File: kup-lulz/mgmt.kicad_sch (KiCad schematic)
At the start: 24 parts, among them J37 XILINX_JTAG, J38 PMOD_HOST, J39 CONN_01X03, U14 STM32L431VxIx, U15 AT24MAC402, U9 XILINX_ULTRASCALEPLUS_B676

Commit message: Continued MCU fanout
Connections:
- net SFP1_MOD_ABS: now also U14.D12 (PC9); no longer U14.G1 (PH1)
- net SFP1_RS0: now also U14.E12 (PC6); no longer U14.M5 (PB0)
- net SFP1_RS1: now also U14.J12 (PD10); no longer U14.M8 (PE9)
- net SFP1_RX_LOS: now also U14.H12 (PD13); no longer U14.M10 (PE13)
- net SFP1_TX_DISABLE: now also U14.C8 (PD2); no longer U14.A12 (PA12)
- net SFP1_TX_FAULT: now also U14.A12 (PA12); no longer U14.M9 (PE11)
- net SFP2_MOD_ABS: now also U14.M7 (PE7); no longer U14.M11 (PE14)
- net SFP2_RS0: now also U14.M5 (PB0); no longer U14.M12 (PE15)
- net SFP2_RS1: now also U14.M9 (PE11); no longer U14.C8 (PD2)
- net SFP2_RX_LOS: now also U14.M10 (PE13); no longer U14.H12 (PD13)
- net SFP2_TX_DISABLE: now also U14.M11 (PE14); no longer U14.M7 (PE7)
- net SFP2_TX_FAULT: now also U14.M12 (PE15); no longer U14.E12 (PC6)
- net SFP3_MOD_ABS: now also U14.G1 (PH1); no longer U14.D12 (PC9)
- net SFP3_TX_FAULT: now also U14.M8 (PE9); no longer U14.J12 (PD10)
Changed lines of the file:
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@@
   (title_block
     (title "Kintex Ultrascale+ OshPark For The Lulz")
-    (date "2024-02-21")
+    (date "2024-02-22")
     (rev "0.1")
     (company "Antikernel Labs")
@@
     (effects (font (size 1.27 1.27)) (justify right))
   )
-  (hierarchical_label "SFP1_RS0" (shape output) (at 102.87 170.18 180)
+  (hierarchical_label "SFP1_RS0" (shape output) (at 153.67 186.69 180)
     (effects (font (size 1.27 1.27)) (justify right))
   )
@@
     (effects (font (size 1.27 1.27)) (justify right))
   )
-  (hierarchical_label "SFP2_MOD_ABS" (shape input) (at 242.57 207.01 180)
+  (hierarchical_label "SFP2_MOD_ABS" (shape input) (at 242.57 189.23 180)
     (effects (font (size 1.27 1.27)) (justify right))
   )
@@
     (effects (font (size 1.27 1.27)) (justify right))
   )
-  (hierarchical_label "SFP1_RX_LOS" (shape input) (at 242.57 204.47 180)
+  (hierarchical_label "SFP1_RX_LOS" (shape input) (at 196.85 204.47 180)
     (effects (font (size 1.27 1.27)) (justify right))
   )
@@
     (effects (font (size 1.27 1.27)) (justify right))
   )
-  (hierarchical_label "SFP2_TX_FAULT" (shape input) (at 153.67 186.69 180)
+  (hierarchical_label "SFP2_TX_FAULT" (shape input) (at 242.57 209.55 180)
     (effects (font (size 1.27 1.27)) (justify right))
   )
@@
     (effects (font (size 1.27 1.27)) (justify right))
   )
-  (hierarchical_label "SFP1_MOD_ABS" (shape input) (at 285.75 194.31 180)
+  (hierarchical_label "SFP1_MOD_ABS" (shape input) (at 153.67 194.31 180)
     (effects (font (size 1.27 1.27)) (justify right))
   )
@@
     (effects (font (size 1.27 1.27)) (justify right))
   )
-  (hierarchical_label "SFP2_RS0" (shape output) (at 242.57 209.55 180)
+  (hierarchical_label "SFP2_RS0" (shape output) (at 102.87 170.18 180)
     (effects (font (size 1.27 1.27)) (justify right))
   )
@@
     (effects (font (size 1.27 1.27)) (justify right))
   )
-  (hierarchical_label "SFP2_RS1" (shape output) (at 196.85 176.53 180)
+  (hierarchical_label "SFP2_RS1" (shape output) (at 242.57 199.39 180)
     (effects (font (size 1.27 1.27)) (justify right))
   )
@@
     (effects (font (size 1.27 1.27)) (justify right))
   )
-  (hierarchical_label "SFP3_MOD_ABS" (shape input) (at 153.67 194.31 180)
+  (hierarchical_label "SFP3_MOD_ABS" (shape input) (at 285.75 194.31 180)
     (effects (font (size 1.27 1.27)) (justify right))
   )
@@
     (effects (font (size 1.27 1.27)) (justify right))
   )
-  (hierarchical_label "SFP3_TX_FAULT" (shape input) (at 196.85 196.85 180)
-    (effects (font (size 1.27 1.27)) (justify right))
-  )
-  (hierarchical_label "SFP1_TX_DISABLE" (shape output) (at 43.18 200.66 180)
+  (hierarchical_label "SFP3_TX_FAULT" (shape input) (at 242.57 194.31 180)
+    (effects (font (size 1.27 1.27)) (justify right))
+  )
+  (hierarchical_label "SFP1_TX_DISABLE" (shape output) (at 196.85 176.53 180)
     (effects (font (size 1.27 1.27)) (justify right))
   )
@@
     (effects (font (size 1.27 1.27)) (justify right))
   )
-  (hierarchical_label "SFP1_TX_FAULT" (shape input) (at 242.57 199.39 180)
+  (hierarchical_label "SFP1_TX_FAULT" (shape input) (at 43.18 200.66 180)
     (effects (font (size 1.27 1.27)) (justify right))
   )
@@
     (effects (font (size 1.27 1.27)) (justify right))
   )
-  (hierarchical_label "SFP2_RX_LOS" (shape input) (at 196.85 204.47 180)
+  (hierarchical_label "SFP2_RX_LOS" (shape input) (at 242.57 204.47 180)
     (effects (font (size 1.27 1.27)) (justify right))
   )
@@
     (effects (font (size 1.27 1.27)) (justify right))
   )
-  (hierarchical_label "SFP1_RS1" (shape output) (at 242.57 194.31 180)
+  (hierarchical_label "SFP1_RS1" (shape output) (at 196.85 196.85 180)
     (effects (font (size 1.27 1.27)) (justify right))
   )
@@
     (effects (font (size 1.27 1.27)) (justify right))
   )
-  (hierarchical_label "SFP2_TX_DISABLE" (shape output) (at 242.57 189.23 180)
-    (effects (font (size 1.27 1.27)) (justify right))
-  )
+  (hierarchical_label "SFP2_TX_DISABLE" (shape output) (at 242.57 207.01 180)
+    (effects (font (size 1.27 1.27)) (justify right))
+  )

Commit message: Updating file: kup-lulz.kicad_pcb with current fully routed design
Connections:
- net MCU_READY: now also U14.F1 (PH0); no longer U14.D1 (PC14)
- net SFP2_MOD_ABS: now also U14.M10 (PE13); no longer U14.M7 (PE7)
- net SFP2_RS0: now also U14.M9 (PE11); no longer U14.M5 (PB0)
- net SFP2_RS1: now also U14.M7 (PE7); no longer U14.M9 (PE11)
- net SFP2_RX_LOS: now also U14.M8 (PE9); no longer U14.M10 (PE13)
- net SFP3_MOD_ABS: now also U14.M5 (PB0); no longer U14.G1 (PH1)
- net SFP3_RS0: now also U14.L6 (PB2); no longer U14.M6 (PB1)
- net SFP3_RS1: now also U14.G1 (PH1); no longer U14.E1 (PC15)
- net SFP3_RX_LOS: now also U14.K5 (PC4); no longer U14.F1 (PH0)
- net SFP3_TX_DISABLE: now also U14.M6 (PB1); no longer U14.K8 (PD9)
- net SFP3_TX_FAULT: now also U14.K8 (PD9); no longer U14.M8 (PE9)
- net SOFT_POWER: now also U14.D1 (PC14); no longer U14.K5 (PC4)
- net SOFT_RESET: now also U14.E1 (PC15); no longer U14.L6 (PB2)
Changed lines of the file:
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@@
     (effects (font (size 1.27 1.27)) (justify right))
   )
-  (hierarchical_label "SFP2_MOD_ABS" (shape input) (at 242.57 189.23 180)
+  (hierarchical_label "SFP2_MOD_ABS" (shape input) (at 242.57 204.47 180)
     (effects (font (size 1.27 1.27)) (justify right))
   )
-  (hierarchical_label "SFP3_RX_LOS" (shape input) (at 285.75 191.77 180)
+  (hierarchical_label "SFP3_RX_LOS" (shape input) (at 153.67 181.61 180)
     (effects (font (size 1.27 1.27)) (justify right))
   )
-  (hierarchical_label "SOFT_POWER" (shape output) (at 153.67 181.61 180)
+  (hierarchical_label "SOFT_POWER" (shape output) (at 153.67 207.01 180)
     (effects (font (size 1.27 1.27)) (justify right))
   )
@@
     (effects (font (size 1.27 1.27)) (justify right))
   )
-  (hierarchical_label "SFP3_RS1" (shape output) (at 153.67 209.55 180)
+  (hierarchical_label "SFP3_RS1" (shape output) (at 285.75 194.31 180)
     (effects (font (size 1.27 1.27)) (justify right))
   )
@@
     (effects (font (size 1.27 1.27)) (justify right))
   )
-  (hierarchical_label "SOFT_RESET" (shape output) (at 102.87 175.26 180)
+  (hierarchical_label "SOFT_RESET" (shape output) (at 153.67 209.55 180)
     (effects (font (size 1.27 1.27)) (justify right))
   )
@@
     (effects (font (size 1.27 1.27)) (justify right))
   )
-  (hierarchical_label "SFP2_RS0" (shape output) (at 102.87 170.18 180)
+  (hierarchical_label "SFP2_RS0" (shape output) (at 242.57 199.39 180)
     (effects (font (size 1.27 1.27)) (justify right))
   )
@@
     (effects (font (size 1.27 1.27)) (justify right))
   )
-  (hierarchical_label "SFP2_RS1" (shape output) (at 242.57 199.39 180)
+  (hierarchical_label "SFP2_RS1" (shape output) (at 242.57 189.23 180)
     (effects (font (size 1.27 1.27)) (justify right))
   )
@@
     (effects (font (size 1.27 1.27)) (justify right))
   )
-  (hierarchical_label "MCU_READY" (shape output) (at 153.67 207.01 180)
+  (hierarchical_label "MCU_READY" (shape output) (at 285.75 191.77 180)
     (effects (font (size 1.27 1.27)) (justify right))
   )
-  (hierarchical_label "SFP3_RS0" (shape output) (at 102.87 172.72 180)
+  (hierarchical_label "SFP3_RS0" (shape output) (at 102.87 175.26 180)
     (effects (font (size 1.27 1.27)) (justify right))
   )
@@
     (effects (font (size 1.27 1.27)) (justify right))
   )
-  (hierarchical_label "SFP3_TX_DISABLE" (shape output) (at 196.85 194.31 180)
+  (hierarchical_label "SFP3_TX_DISABLE" (shape output) (at 102.87 172.72 180)
     (effects (font (size 1.27 1.27)) (justify right))
   )
-  (hierarchical_label "SFP3_MOD_ABS" (shape input) (at 285.75 194.31 180)
+  (hierarchical_label "SFP3_MOD_ABS" (shape input) (at 102.87 170.18 180)
     (effects (font (size 1.27 1.27)) (justify right))
   )
@@
     (effects (font (size 1.27 1.27)) (justify right))
   )
-  (hierarchical_label "SFP3_TX_FAULT" (shape input) (at 242.57 194.31 180)
+  (hierarchical_label "SFP3_TX_FAULT" (shape input) (at 196.85 194.31 180)
     (effects (font (size 1.27 1.27)) (justify right))
   )
@@
     (effects (font (size 1.27 1.27)) (justify right))
   )
-  (hierarchical_label "SFP2_RX_LOS" (shape input) (at 242.57 204.47 180)
+  (hierarchical_label "SFP2_RX_LOS" (shape input) (at 242.57 194.31 180)
     (effects (font (size 1.27 1.27)) (justify right))
   )

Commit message: Finished resolving all first-pass DRC errors (but not warnings)
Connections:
- net SFP0_RS1: now also U9.C11 (IO_L12P_AD0P_86); no longer U9.D14 (IO_L8P_HDGC_87)
- net SFP0_RX_LOS: now also U9.E11 (IO_L7P_HDGC_AD5P_86); no longer U9.H14 (IO_L3P_AD13P_87)
- net SFP1_I2C_SCL: now also U9.H14 (IO_L3P_AD13P_87); no longer U9.C11 (IO_L12P_AD0P_86)
- net SFP1_I2C_SDA: now also U9.D14 (IO_L8P_HDGC_87); no longer U9.E11 (IO_L7P_HDGC_AD5P_86)
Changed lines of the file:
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@@
     (effects (font (size 1.27 1.27)) (justify right))
   )
-  (hierarchical_label "SFP0_RS1" (shape output) (at 36.83 85.09 180)
+  (hierarchical_label "SFP0_RS1" (shape output) (at 101.6 64.77 180)
     (effects (font (size 1.27 1.27)) (justify right))
   )
@@
     (effects (font (size 1.27 1.27)) (justify right))
   )
-  (hierarchical_label "SFP1_I2C_SDA" (shape bidirectional) (at 101.6 90.17 180)
+  (hierarchical_label "SFP1_I2C_SDA" (shape bidirectional) (at 36.83 85.09 180)
     (effects (font (size 1.27 1.27)) (justify right))
   )
@@
     (effects (font (size 1.27 1.27)) (justify right))
   )
-  (hierarchical_label "SFP0_RX_LOS" (shape input) (at 36.83 110.49 180)
+  (hierarchical_label "SFP0_RX_LOS" (shape input) (at 101.6 90.17 180)
     (effects (font (size 1.27 1.27)) (justify right))
   )
@@
     (effects (font (size 1.27 1.27)) (justify right))
   )
-  (hierarchical_label "SFP1_I2C_SCL" (shape output) (at 101.6 64.77 180)
+  (hierarchical_label "SFP1_I2C_SCL" (shape output) (at 36.83 110.49 180)
     (effects (font (size 1.27 1.27)) (justify right))
   )

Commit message: Converted to kicad8 format, updated footprints and 3D models appropriately
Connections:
- net QSFP0_I2C_SEL_N: now also U9.E12 (IO_L7N_HDGC_87); no longer U9.A9 (IO_L10N_AD2N_86)
- net QSFP0_INT_N: now also U9.B10 (IO_L11P_AD1P_86); no longer U9.A12 (IO_L11N_AD9N_87)
- net QSFP0_LPMODE: now also U9.C12 (IO_L10P_AD10P_87); no longer U9.B9 (IO_L10P_AD2P_86)
- net QSFP0_PRESENT_N: now also U9.A10 (IO_L11N_AD1N_86); no longer U9.B12 (IO_L10N_AD10N_87)
- net QSFP0_RST_N: now also U9.F12 (IO_L5N_HDGC_87); no longer U9.B10 (IO_L11P_AD1P_86)
- net QSFP1_I2C_SEL_N: now also U9.B11 (IO_L12N_AD0N_86); no longer U9.A13 (IO_L11P_AD9P_87)
- net QSFP1_INT_N: now also U9.A13 (IO_L11P_AD9P_87); no longer U9.C12 (IO_L10P_AD10P_87)
- net QSFP1_LPMODE: now also U9.B12 (IO_L10N_AD10N_87); no longer U9.A14 (IO_L12N_AD8N_87)
- net QSFP1_PRESENT_N: now also U9.B14 (IO_L12P_AD8P_87); no longer U9.E12 (IO_L7N_HDGC_87)
- net QSFP1_RST_N: now also U9.A12 (IO_L11N_AD9N_87); no longer U9.B14 (IO_L12P_AD8P_87)
- net QSFP_I2C_SCL: now also U9.B9 (IO_L10P_AD2P_86); no longer U9.A10 (IO_L11N_AD1N_86)
- net QSFP_I2C_SDA: now also U9.A9 (IO_L10N_AD2N_86); no longer U9.B11 (IO_L12N_AD0N_86)
- net SFP0_I2C_SCL: now also U9.C14 (IO_L9P_AD11P_87); no longer U9.G12 (IO_L5P_HDGC_87)
- net SFP0_I2C_SDA: now also U9.A14 (IO_L12N_AD8N_87); no longer U9.E13 (IO_L7P_HDGC_87)
- net SFP0_MOD_ABS: now also U9.E13 (IO_L7P_HDGC_87); no longer U9.F14 (IO_L6P_HDGC_87)
- net SFP0_RS0: now also U9.G12 (IO_L5P_HDGC_87); no longer U9.G14 (IO_L3N_AD13N_87)
- net SFP0_RS1: now also U9.G14 (IO_L3N_AD13N_87); no longer U9.C11 (IO_L12P_AD0P_86)
- net SFP0_RX_LOS: now also U9.F14 (IO_L6P_HDGC_87); no longer U9.E11 (IO_L7P_HDGC_AD5P_86)
- net SFP0_TX_DISABLE: now also U9.C11 (IO_L12P_AD0P_86); no longer U9.F12 (IO_L5N_HDGC_87)
- net SFP0_TX_FAULT: now also U9.E11 (IO_L7P_HDGC_AD5P_86); no longer U9.C14 (IO_L9P_AD11P_87)

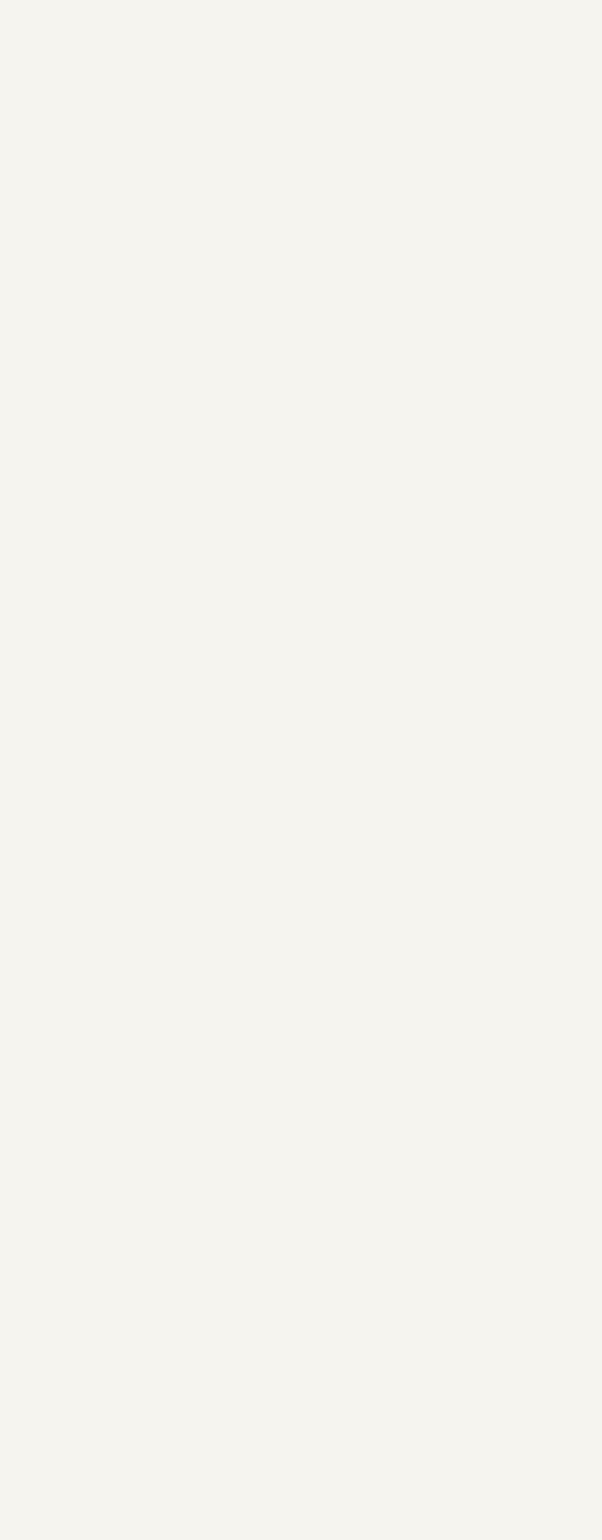
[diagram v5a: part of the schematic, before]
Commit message: Replaced supervisor with L431
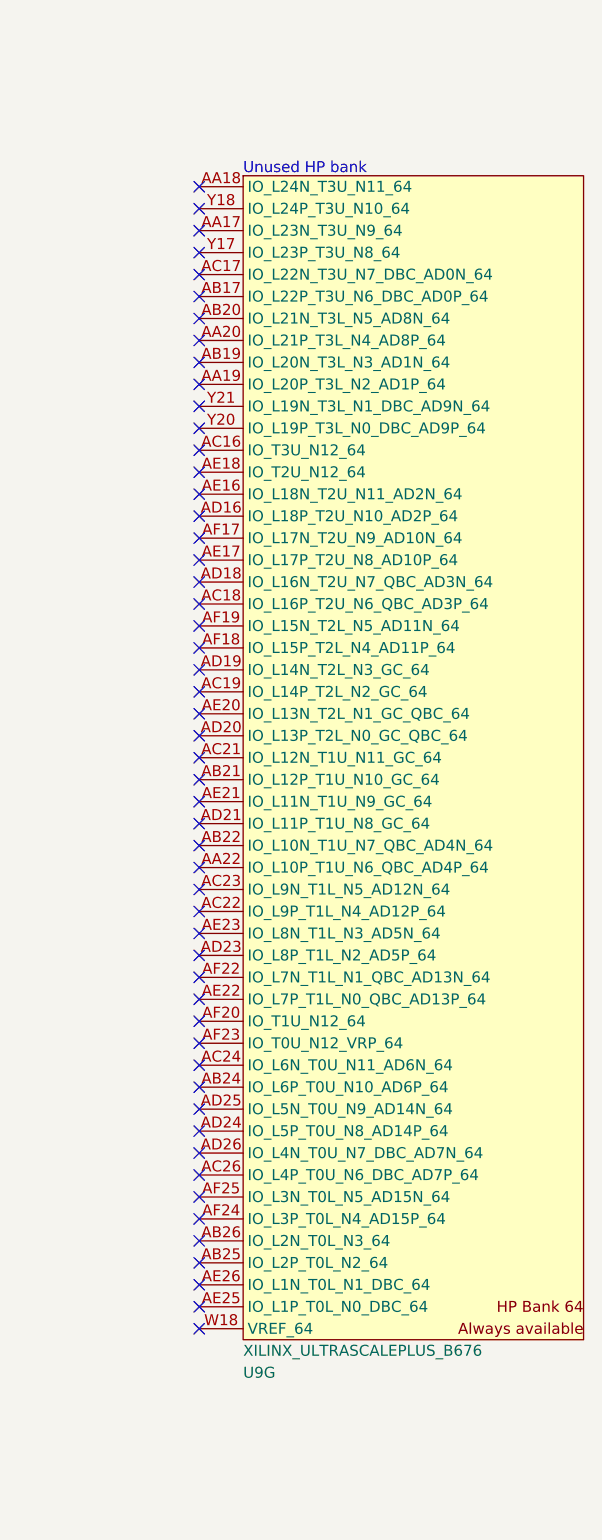
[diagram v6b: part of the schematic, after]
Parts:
- added unit 7 of U9
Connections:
- no-connect marks 81 -> 134
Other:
- note added: "Unused HP bank"

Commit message: Continued MCU routing
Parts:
- removed J37: XILINX_JTAG, azonenberg_pcb:XILINX_JTAG_PTH_MOLEX_0878311420, symbol xilinx-azonenberg:XILINX_JTAG
- removed U14: STM32L431VxIx, azonenberg_pcb:BGA_100_7x7_DEPOP_0.5MM_STM32_UFBGA100_OSHPARK, symbol st-azonenberg:STM32L431VxIx
- added C144: 22 uF, azonenberg_pcb:EIA_0805_CAP_NOSILK, symbol device:C
- added C145, C146, C147, C148, C149, C150, C151, C152, C153: 0.47 uF, azonenberg_pcb:EIA_0402_CAP_NOSILK, symbol device:C
- added C154, C156, C36: 10 uF, azonenberg_pcb:EIA_0805_CAP_NOSILK, symbol device:C
- added C155: 220 pF, azonenberg_pcb:EIA_0402_CAP_NOSILK, symbol device:C
- added C28, C32: 4.7 uF, azonenberg_pcb:EIA_0603_CAP_NOSILK, symbol device:C
- added D5, D6, D7, D8: GREEN, azonenberg_pcb:EIA_0402_LED, symbol device:LED
- added J4: CORTEX_DEBUG_ETM, azonenberg_pcb:CONN_HEADER_1.27MM_2x10_SMT_SAMTEC_FTSH-110-01-L-DV-K, symbol special-azonenberg:CORTEX_DEBUG_ETM
- added L15: 2.2 uH, azonenberg_pcb:EIA_1210_CAP_NOSILK, symbol passive-azonenberg:INDUCTOR_PWROUT
- added R36: 33, azonenberg_pcb:EIA_0402_RES_NOSILK, symbol device:R
- added R37, R58: 10K, azonenberg_pcb:EIA_0402_RES_NOSILK, symbol device:R
- added R59, R98, R99: 33K, azonenberg_pcb:EIA_0402_RES_NOSILK, symbol device:R
- added TP17, TP26, TP5: U.FL, azonenberg_pcb:CONN_U.FL_TE_1909763-1, symbol conn:CONN_COAXIAL
- added U14: STM32H735-UFBGA176-25, azonenberg_pcb:BGA_201_10x10_DEPOP_0.65MM_OSHPARK, symbol st-azonenberg:STM32H735-UFBGA176-25
- added U6: ECS-1612MV-250-CN, azonenberg_pcb:OSCILLATOR_1.6x1.2, symbol osc-azonenberg:OSC
- C124: value 4.7 uF -> 2.2 uF; footprint azonenberg_pcb:EIA_0603_CAP_NOSILK -> azonenberg_pcb:EIA_0805_CAP_NOSILK
- C127, C129: value 0.47 uF -> 4.7 uF; footprint azonenberg_pcb:EIA_0402_CAP_NOSILK -> azonenberg_pcb:EIA_0603_CAP_NOSILK
- C128: value 0.47 uF -> 2.2 uF; footprint azonenberg_pcb:EIA_0402_CAP_NOSILK -> azonenberg_pcb:EIA_0805_CAP_NOSILK
- R93: value 10K -> 33K
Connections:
- net 3V3: now also C125.1, C127.1, C132.2, C144.1, C145.1, C146.2, C147.1, C148.2, C149.1, C150.2, C151.1, C152.2, C153.1, C28.1, C36.1, J4.1 (VCC), R58.2, U14.D11 (VDD), U14.D4 (PDR_ON), U14.D5 (VDD), U14.E12 (VDD), U14.E15 (VDD50USB), U14.E4 (VDD), U14.F13 (VDD33USB), U14.G1 (VDDSMPS), U14.G4 (VDD), U14.H12 (VDD), U14.K4 (VDD), U14.L12 (VDD), U14.M3 (VREF+), U14.M5 (VDD), U14.M9 (VDD), U6.1 (E/D#), U6.4 (Vdd); no longer C124.1, C126.1, C128.1, C129.1, C132.1, C133.1
- net GND: now also C132.1, C144.2, C145.2, C146.1, C147.2, C148.1, C149.2, C150.1, C151.2, C152.1, C153.2, C154.2, C155.2, C156.2, C28.2, C32.2, C36.2, D5.1 (K), D6.1 (K), D7.1 (K), D8.1 (K), J4.11 (GND), J4.13 (GND), J4.15 (GND), J4.17 (GND), J4.19 (GND), J4.3 (GND), J4.5 (GND), J4.9 (GNDdet), R37.1, TP17.2 (Ext), TP26.2 (Ext), TP5.2 (Ext), U14.A1 (VSS), U14.A15 (VSS), U14.C2 (VSS), U14.D10 (VSS), U14.D6 (VSS), U14.E1 (VSS), U14.F10 (VSS), U14.F12 (VSS), U14.F2 (VSSSMPS), U14.F6 (VSS), U14.F7 (VSS), U14.F8 (VSS), U14.F9 (VSS), U14.G10 (VSS), U14.G6 (VSS), U14.G7 (VSS), U14.G8 (VSS), U14.G9 (VSS), U14.H10 (VSS), U14.H6 (VSS), U14.H7 (VSS), U14.H8 (VSS), U14.H9 (VSS), U14.J10 (VSS), U14.J14 (VSS), U14.J6 (VSS), U14.J7 (VSS), U14.J8 (VSS), U14.J9 (VSS), U14.K10 (VSS), U14.K12 (VSS), U14.K2 (VSS), U14.K6 (VSS), U14.K7 (VSS), U14.K8 (VSS), U14.K9 (VSS), U14.L4 (VREF-), U14.M10 (VSS), U14.M6 (VSS), U14.N3 (VSSA), U14.R1 (VSS), U14.R15 (VSS), U6.2 (Vss); no longer C132.2, R93.2
- net I2C_SCL: now also U14.R5 (PH5)
- net I2C_SDA: now also U14.P4 (PH4)
- net MCU_JTAG_TCK: now also J4.4 (TCK), U14.A12 (PA14)
- net MCU_JTAG_TDI: now also J4.8 (TDI), U14.A11 (PA15)
- net MCU_JTAG_TDO: now also J4.6 (TDO)
- net MCU_JTAG_TMS: now also J4.2 (TMS), U14.B13 (PA13)
- net MCU_PMOD_DQ0: now also U14.R6 (PC4)
- net MCU_PMOD_DQ1: now also U14.C6 (PB5)
- net MCU_PMOD_DQ2: now also U14.P1 (PA0)
- net MCU_PMOD_DQ3: now also U14.B5 (PB7)
- net MCU_PMOD_DQ4: now also U14.C7 (PG14)
- net MCU_PMOD_DQ5: now also U14.P7 (PB2)
- net MCU_PMOD_DQ6: now also U14.R7 (PA6)
- net MCU_PMOD_DQ7: now also U14.A5 (PB6)
- net MCU_READY: now also U14.P6 (PA5)
- net MCU_RST_N: now also J4.10 (~{RST}), U14.L1 (NRST)
- net MCU_UART_RX: now also U14.C15 (PA11)
- net MCU_UART_TX: now also U14.B15 (PA12)
- net MCU_VDDA: now also C129.1, C133.1, TP26.1 (In), U14.M4 (VDDA); no longer C125.1, C127.1
- net MGMT_SPI_CS_N: now also U9.W15 (IO_L10N_AD2N_84), U14.D8 (PG12); no longer U9.W14 (IO_L10P_AD2P_84)
- net MGMT_SPI_SCK: now also U14.H2 (PF4)
- net SFP1_MOD_ABS: now also U14.A8 (PG9)
- net SFP1_RS0: now also U14.B9 (PD5)
- net SFP1_RS1: now also U14.B10 (PD2)
- net SFP1_RX_LOS: now also U14.A9 (PD3)
- net SFP1_TX_DISABLE: now also U14.C9 (PD4)
- net SFP1_TX_FAULT: now also U14.C8 (PG10)
- net SFP2_I2C_SCL: now also U14.C11 (PC11)
- net SFP2_I2C_SDA: now also U14.C12 (PC10)
- net SFP2_MOD_ABS: now also U14.B12 (PH14)
- net SFP2_RS0: now also U14.B14 (PA8)
- net SFP2_RS1: now also U14.D15 (PC7)
- net SFP2_RX_LOS: now also U14.D14 (PC8)
- net SFP2_TX_DISABLE: now also U14.C10 (PD0)
- net SFP2_TX_FAULT: now also U14.A10 (PD1)
- net SFP3_I2C_SCL: now also U14.J15 (PD12)
- net SFP3_I2C_SDA: now also U14.H15 (PD13)
- net SFP3_MOD_ABS: now also U14.F15 (PG5)
- net SFP3_RS0: now also U14.G14 (PG4)
- net SFP3_RS1: now also U14.K15 (PB14)
- net SFP3_RX_LOS: now also U14.G15 (PG2)
- net SFP3_TX_DISABLE: now also U14.H14 (PD14)
- net SFP3_TX_FAULT: now also U14.F14 (PG6)
- net SOFT_POWER: now also U14.R2 (PA2)
- net SOFT_RESET: now also U14.M7 (PC5)
- net SUPER_SPI_CS_N: now also U14.H1 (PF6)
- net SUPER_SPI_MISO: now also U14.J2 (PF8)
- net SUPER_SPI_MOSI: now also U14.J4 (PF9)
- net SUPER_SPI_SCK: now also U14.J3 (PF7)
- net at R92.2: now also U14.A6 (PB3)
- net MGMT_SPI_DQS: now reaches U9.AA13 (IO_L11N_AD1N_84)
- net MGMT_SPI_DQS: now also U14.D7 (PG15)
- net MGMT_SPI_DQ2: now reaches U9.W13 (IO_L12N_AD0N_84)
- net MGMT_SPI_DQ2: now also U14.G3 (PF2)
- net MGMT_SPI_DQ3: now reaches U9.Y15 (IO_L7P_HDGC_AD5P_84)
- net MGMT_SPI_DQ3: now also U14.H4 (PF3)
- net MCU_LED_1: now reaches R93.1
- net MCU_LED_1: now also U14.M15 (PB12)
- net MGMT_SPI_MISO renamed MGMT_SPI_DQ0
- net MGMT_SPI_DQ0: now also U14.F4 (PF0)
- net MGMT_SPI_MOSI renamed MGMT_SPI_DQ1
- net MGMT_SPI_DQ1: now also U14.F3 (PF1)
- new net: R36.2, U6.3 (CLK)
- new net: D6.2 (A), R93.2
- new net: D7.2 (A), R98.2
- new net: D8.2 (A), R99.2
- new net: D5.2 (A), R59.2
- new net 3V3_SB: C126.1, U14.E2 (VBAT)
- new net MCU_BOOT0: R37.2, U14.C5 (BOOT0)
- new net MCU_CLK_25MHZ: R36.1, U14.J1 (PH0)
- new net MCU_JTAG_TRST: R58.1, U14.B6 (PB4)
- new net MCU_LED_0: R59.1, U14.L15 (PB13)
- new net MCU_LED_2: R98.1, U14.N15 (PH12)
- new net MCU_LED_3: R99.1, U14.P15 (PH6)
- new net VCORE: C124.1, C128.1, TP5.1 (In), U14.A14 (VCAP), U14.A4 (VCAP), U14.R13 (VCAP)
- new net VLXSMPS: C155.1, L15.2, U14.F1 (VLXSMPS)
- new net VSMPS: C154.1, C156.1, C32.1, L15.1, TP17.1 (In), U14.A13 (VDDLDO), U14.A3 (VDDLDO), U14.G2 (VFBSMPS), U14.R14 (VDDLDO)
- no-connect marks 134 -> 175
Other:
- note added: "MCU VBAT decoupling"
- note added: "MCU VCAP decoupling"
- note added: "MCU VDD decoupling"
- note added: "MCU VDDLDO decoupling"
- note added: "MCU VDDSMPS decoupling"
- moved on the sheet: J39, R92
